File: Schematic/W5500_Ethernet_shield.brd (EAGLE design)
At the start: 68.6 x 53.3 mm, 97 parts, among them P1 57-00013QL11-1, P2 7MSDP-B0-1012, U1 W5500, U2 AME8815, U3 SN74LVC1G125, U4 SN74LVC1G125, U5 SN74LVC1G125, U6 SN74LVC1G125, U7 SN74LVC1G125, U8 SN74LVC1G125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

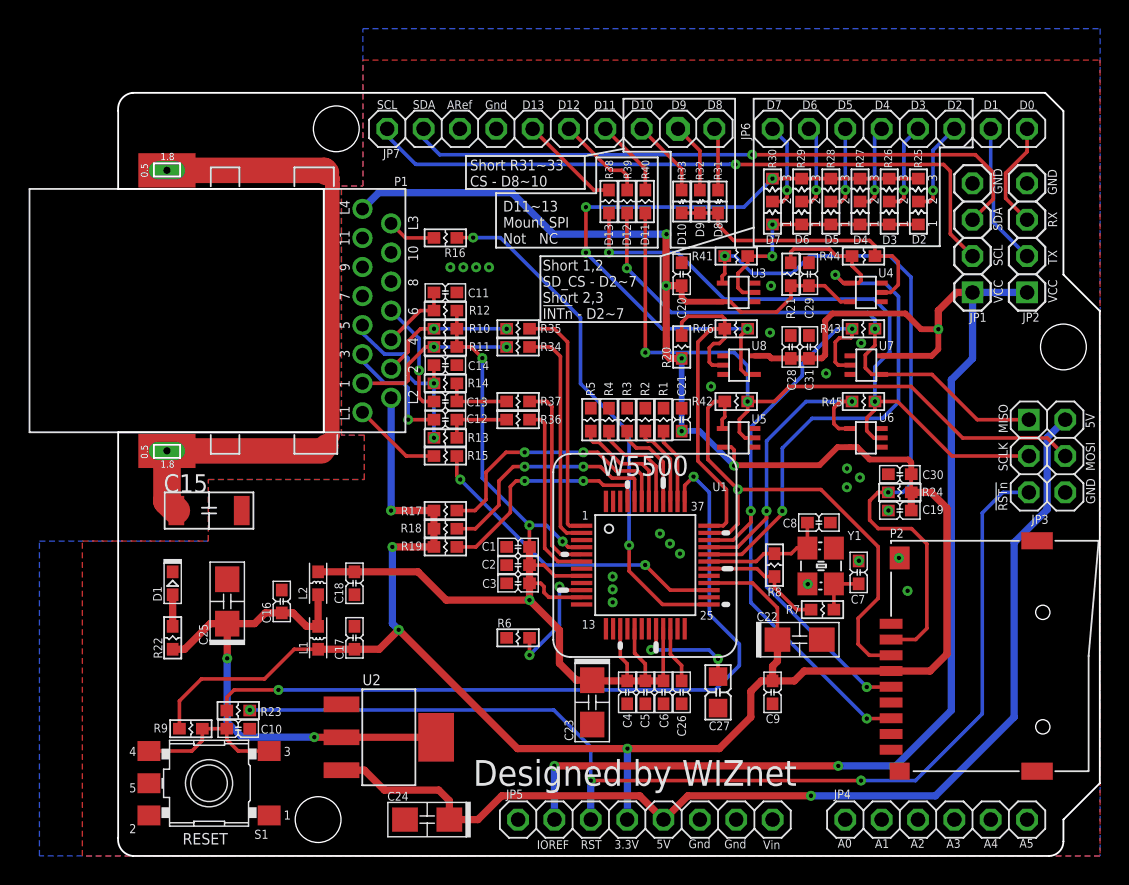
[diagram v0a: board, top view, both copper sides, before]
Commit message: Update to Rev1.1 files
In Rev 1.0, GND pin of “RESET” button(S1) was floating.
This change in Rev1.1 will solve the floating problem. (Connect to GND
with adding VIA.)
Refer to below picture.
GND is reinforced by adding via hole to whole board
Via located was close to D11 pattern(R20). so that via is separated.
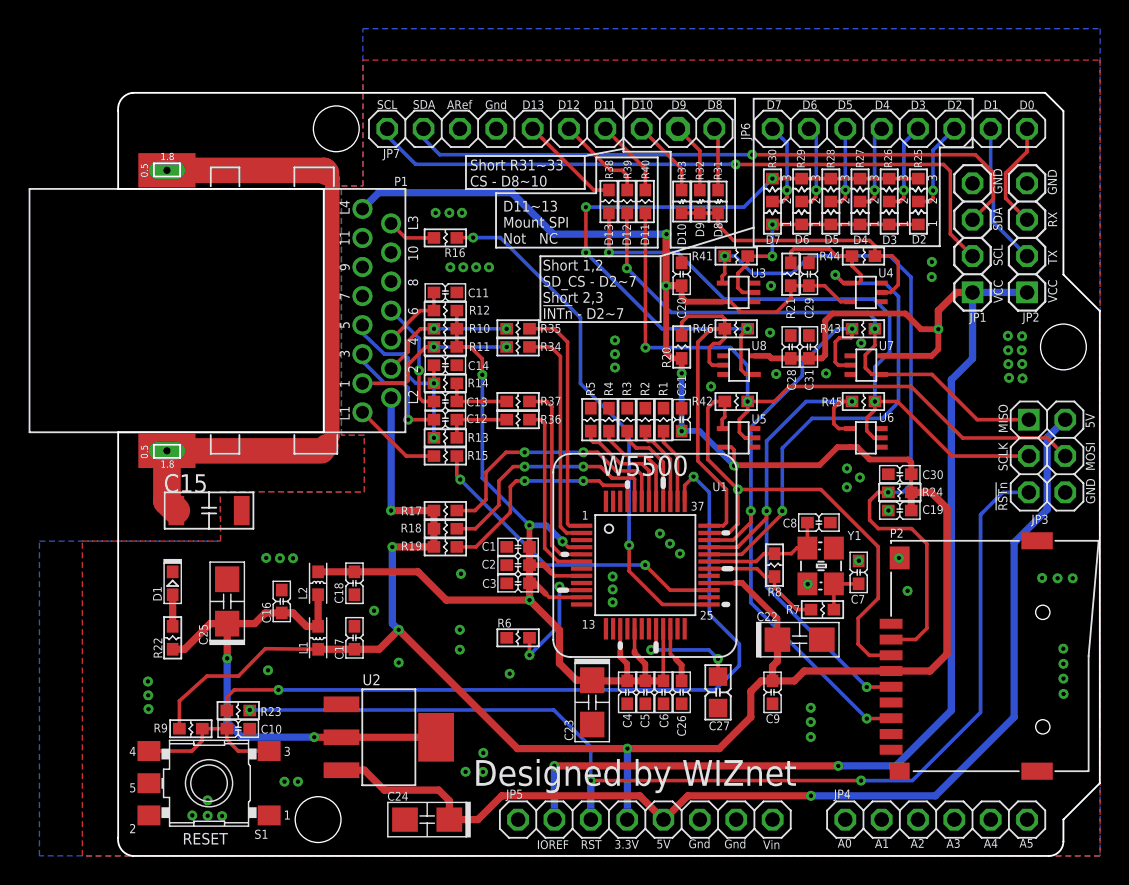
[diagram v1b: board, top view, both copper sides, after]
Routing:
- net +3V3: track 192.8 -> 192.3 mm
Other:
- board text added: "BOARD MODEL W5500 ETHERNET SHIELD V1.1"
- board text removed: "BOARD MODEL W5500 ETHERNET SHIELD V1.0"
